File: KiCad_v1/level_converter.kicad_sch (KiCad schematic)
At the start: 3 parts, among them Q1 BSS138

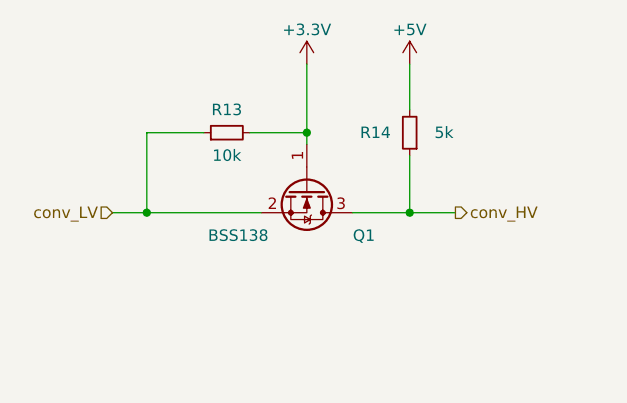
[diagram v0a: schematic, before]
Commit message: Level converter changed to 74LV1T34
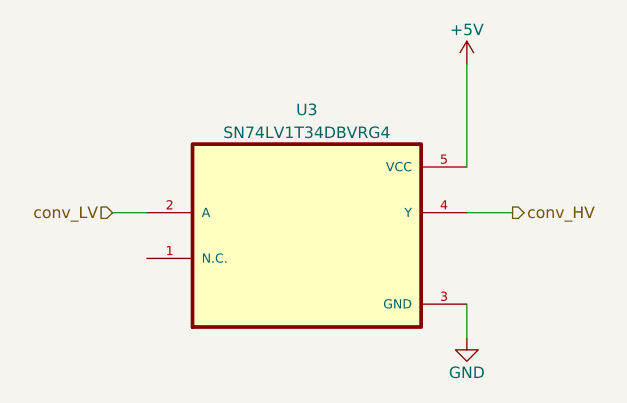
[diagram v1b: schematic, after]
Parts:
- removed Q1: BSS138, Package_TO_SOT_SMD:SOT-23, symbol Transistor_FET:BSS138
- removed R13: 10k, Resistor_SMD:R_0603_1608Metric_Pad0.98x0.95mm_HandSolder, symbol Device:R_Small
- removed R14: 5k, Resistor_SMD:R_0603_1608Metric_Pad0.98x0.95mm_HandSolder, symbol Device:R_Small
- added U3: SN74LV1T34DBVRG4, SOT95P280X145-5N, symbol sharp-ce140f-emul:SN74LV1T34DBVRG4
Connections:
- net +5V: now also U3.5 (VCC)
- net conv_HV: now also U3.4 (Y)
- net conv_LV: now also U3.2 (A)
- new net GND: U3.3 (GND)
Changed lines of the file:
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@@
-(kicad_sch (version 20211123) (generator eeschema)
+(kicad_sch (version 20230121) (generator eeschema)
   (paper "A5")
   (title_block
@@
     (rev "1")
     (comment 1 "https://www.sparkfun.com/products/12009")
-    (comment 2 "Bi-directional logic level converter")
+    (comment 2 "Single Power Supply Single Buffer GATE CMOS Logic Level Shifter")
   )
-  (junction (at 101.6 60.96) (diameter 0) (color 0 0 0 0)
+  (wire (pts (xy 119.38 69.85) (xy 124.46 69.85))
+    (stroke (width 0) (type default))
   )
-  (junction (at 83.82 69.85) (diameter 0) (color 0 0 0 0)
-  )
-  (junction (at 113.03 69.85) (diameter 0) (color 0 0 0 0)
-  )
-  (wire (pts (xy 113.03 69.85) (xy 118.11 69.85))
-    (stroke (width 0) (type default) (color 0 0 0 0))
-  )
-  (wire (pts (xy 83.82 60.96) (xy 90.17 60.96))
-    (stroke (width 0) (type default) (color 0 0 0 0))
-  )
-  (wire (pts (xy 113.03 53.34) (xy 113.03 58.42))
-    (stroke (width 0) (type default) (color 0 0 0 0))
-  )
-  (wire (pts (xy 95.25 60.96) (xy 101.6 60.96))
-    (stroke (width 0) (type default) (color 0 0 0 0))
-  )
-  (wire (pts (xy 101.6 53.34) (xy 101.6 60.96))
-    (stroke (width 0) (type default) (color 0 0 0 0))
-  )
-  (wire (pts (xy 113.03 63.5) (xy 113.03 69.85))
-    (stroke (width 0) (type default) (color 0 0 0 0))
-  )
-  (wire (pts (xy 83.82 69.85) (xy 96.52 69.85))
-    (stroke (width 0) (type default) (color 0 0 0 0))
-  )
-  (wire (pts (xy 101.6 60.96) (xy 101.6 62.23))
-    (stroke (width 0) (type default) (color 0 0 0 0))
-  )
-  (wire (pts (xy 83.82 69.85) (xy 83.82 60.96))
-    (stroke (width 0) (type default) (color 0 0 0 0))
-  )
-  (wire (pts (xy 106.68 69.85) (xy 113.03 69.85))
-    (stroke (width 0) (type default) (color 0 0 0 0))
+  (wire (pts (xy 119.38 80.01) (xy 119.38 83.82))
+    (stroke (width 0) (type default))
   )
   (wire (pts (xy 80.01 69.85) (xy 83.82 69.85))
-    (stroke (width 0) (type default) (color 0 0 0 0))
+    (stroke (width 0) (type default))
   )
-  (hierarchical_label "conv_HV" (shape output) (at 118.11 69.85 0)
+  (wire (pts (xy 119.38 53.34) (xy 119.38 64.77))
+    (stroke (width 0) (type default))
+  )
+  (hierarchical_label "conv_HV" (shape output) (at 124.46 69.85 0) (fields_autoplaced)
     (effects (font (size 1.27 1.27)) (justify left))
   )
-  (hierarchical_label "conv_LV" (shape input) (at 80.01 69.85 180)
+  (hierarchical_label "conv_LV" (shape input) (at 80.01 69.85 180) (fields_autoplaced)
     (effects (font (size 1.27 1.27)) (justify right))
   )
-  (symbol (lib_id "power:+5V") (at 113.03 53.34 0) (unit 1)
-    (in_bom yes) (on_board yes)
-    (property "Reference" "#PWR020" (id 0) (at 113.03 57.15 0)
+  (symbol (lib_id "power:+5V") (at 119.38 53.34 0) (unit 1)
+    (in_bom yes) (on_board yes) (dnp no)
+    (property "Reference" "#PWR020" (at 119.38 57.15 0)
       (effects (font (size 1.27 1.27)) hide)
     )
-    (property "Value" "+5V" (id 1) (at 113.03 49.53 0))
-    (property "Footprint" "" (id 2) (at 113.03 53.34 0)
+    (property "Value" "+5V" (at 119.38 49.53 0)
+      (effects (font (size 1.27 1.27)))
+    )
+    (property "Footprint" "" (at 119.38 53.34 0)
       (effects (font (size 1.27 1.27)) hide)
     )
-    (property "Datasheet" "" (id 3) (at 113.03 53.34 0)
+    (property "Datasheet" "" (at 119.38 53.34 0)
       (effects (font (size 1.27 1.27)) hide)
     )
     (pin "1")
+    (instances
+      (project "sharp-ce140f-emul_v1"
+        (path "/a1aa6218-39ed-4b37-9200-4448085ec785/ec3bcf54-6c70-4868-a3e2-d07f7ca44b3e"
+          (reference "#PWR020") (unit 1)
+        )
+        (path "/a1aa6218-39ed-4b37-9200-4448085ec785/a1077ba1-f425-4ad2-aac3-499598bb8fea"
+          (reference "#PWR0101") (unit 1)
+        )
+        (path "/a1aa6218-39ed-4b37-9200-4448085ec785/ce88f271-4809-4aaa-8ab4-efdfc9a3cf18"
+          (reference "#PWR0102") (unit 1)
+        )
+        (path "/a1aa6218-39ed-4b37-9200-4448085ec785/10a7e6a0-6c73-4880-bece-d370b7dbb5d0"
+          (reference "#PWR0103") (unit 1)
+        )
+        (path "/a1aa6218-39ed-4b37-9200-4448085ec785/f63beab0-aa70-4631-88ee-9ebb92c922a4"
+          (reference "#PWR0104") (unit 1)
+        )
+      )
+    )
   )
-  (symbol (lib_id "Device:R_Small") (at 92.71 60.96 90) (unit 1)
-    (in_bom yes) (on_board yes)
-    (property "Reference" "R13" (id 0) (at 92.71 58.42 90))
-    (property "Value" "10k" (id 1) (at 92.71 63.5 90))
-    (property "Footprint" "Resistor_SMD:R_0603_1608Metric_Pad0.98x0.95mm_HandSolder" (id 2) (at 92.71 60.96 0)
-      (effects (font (size 1.27 1.27)) hide)
+  (symbol (lib_id "sharp-ce140f-emul:SN74LV1T34DBVRG4") (at 101.6 72.39 0) (unit 1)
+    (in_bom yes) (on_board yes) (dnp no) (fields_autoplaced)
+    (property "Reference" "U3" (at 101.6 58.42 0)
+      (effects (font (size 1.27 1.27)))
     )
-    (property "Datasheet" "~" (id 3) (at 92.71 60.96 0)
+    (property "Value" "SN74LV1T34DBVRG4" (at 101.6 60.96 0)
+      (effects (font (size 1.27 1.27)))
+    )
+    (property "Footprint" "SOT95P280X145-5N" (at 101.6 72.39 0)
+      (effects (font (size 1.27 1.27)) (justify bottom) hide)
+    )
+    (property "Datasheet" "" (at 101.6 72.39 0)
       (effects (font (size 1.27 1.27)) hide)
     )
     (pin "1")
     (pin "2")
+    (pin "3")
+    (pin "4")
+    (pin "5")
+    (instances
+      (project "sharp-ce140f-emul_v1"
+        (path "/a1aa6218-39ed-4b37-9200-4448085ec785/ec3bcf54-6c70-4868-a3e2-d07f7ca44b3e"
+          (reference "U3") (unit 1)
+        )
+        (path "/a1aa6218-39ed-4b37-9200-4448085ec785/a1077ba1-f425-4ad2-aac3-499598bb8fea"
+          (reference "U4") (unit 1)
+        )
+        (path "/a1aa6218-39ed-4b37-9200-4448085ec785/ce88f271-4809-4aaa-8ab4-efdfc9a3cf18"
+          (reference "U5") (unit 1)
+        )
+        (path "/a1aa6218-39ed-4b37-9200-4448085ec785/10a7e6a0-6c73-4880-bece-d370b7dbb5d0"
+          (reference "U6") (unit 1)
+        )
+        (path "/a1aa6218-39ed-4b37-9200-4448085ec785/f63beab0-aa70-4631-88ee-9ebb92c922a4"
+          (reference "U7") (unit 1)
+        )
+      )
+    )
   )
-  (symbol (lib_id "Transistor_FET:BSS138") (at 101.6 67.31 270) (unit 1)
-    (in_bom yes) (on_board yes)
-    (property "Reference" "Q1" (id 0) (at 107.95 72.39 90))
-    (property "Value" "BSS138" (id 1) (at 93.98 72.39 90))
-    (property "Footprint" "Package_TO_SOT_SMD:SOT-23" (id 2) (at 99.695 72.39 0)
-      (effects (font (size 1.27 1.27) italic) (justify left) hide)
-    )
-    (property "Datasheet" "https://www.onsemi.com/pub/Collateral/BSS138-D.PDF" (id 3) (at 101.6 67.31 0)
-      (effects (font (size 1.27 1.27)) (justify left) hide)
-    )
-    (pin "1")
-    (pin "2")
-    (pin "3")
-  )
-  (symbol (lib_id "power:+3.3V") (at 101.6 53.34 0) (unit 1)
-    (in_bom yes) (on_board yes)
-    (property "Reference" "#PWR019" (id 0) (at 101.6 57.15 0)
+  (symbol (lib_id "power:GND") (at 119.38 83.82 0) (mirror y) (unit 1)
+    (in_bom yes) (on_board yes) (dnp no)
+    (property "Reference" "#PWR07" (at 119.38 90.17 0)
       (effects (font (size 1.27 1.27)) hide)
     )
-    (property "Value" "+3.3V" (id 1) (at 101.6 49.53 0))
-    (property "Footprint" "" (id 2) (at 101.6 53.34 0)
+    (property "Value" "GND" (at 119.38 87.63 0)
+      (effects (font (size 1.27 1.27)))
+    )
+    (property "Footprint" "" (at 119.38 83.82 0)
       (effects (font (size 1.27 1.27)) hide)
     )
-    (property "Datasheet" "" (id 3) (at 101.6 53.34 0)
+    (property "Datasheet" "" (at 119.38 83.82 0)
       (effects (font (size 1.27 1.27)) hide)
     )
     (pin "1")
-  )
-  (symbol (lib_id "Device:R_Small") (at 113.03 60.96 180) (unit 1)
-    (in_bom yes) (on_board yes)
-    (property "Reference" "R14" (id 0) (at 109.22 60.96 0))
-    (property "Value" "5k" (id 1) (at 116.84 60.96 0))
-    (property "Footprint" "Resistor_SMD:R_0603_1608Metric_Pad0.98x0.95mm_HandSolder" (id 2) (at 113.03 60.96 0)
-      (effects (font (size 1.27 1.27)) hide)
+    (instances
+      (project "sharp-ce140f-emul_v1"
+        (path "/a1aa6218-39ed-4b37-9200-4448085ec785"
+          (reference "#PWR07") (unit 1)
+        )
+        (path "/a1aa6218-39ed-4b37-9200-4448085ec785/ec3bcf54-6c70-4868-a3e2-d07f7ca44b3e"
+          (reference "#PWR019") (unit 1)
+        )
+        (path "/a1aa6218-39ed-4b37-9200-4448085ec785/a1077ba1-f425-4ad2-aac3-499598bb8fea"
+          (reference "#PWR021") (unit 1)
+        )
+        (path "/a1aa6218-39ed-4b37-9200-4448085ec785/ce88f271-4809-4aaa-8ab4-efdfc9a3cf18"
+          (reference "#PWR022") (unit 1)
+        )
+        (path "/a1aa6218-39ed-4b37-9200-4448085ec785/10a7e6a0-6c73-4880-bece-d370b7dbb5d0"
+          (reference "#PWR023") (unit 1)
+        )
+        (path "/a1aa6218-39ed-4b37-9200-4448085ec785/f63beab0-aa70-4631-88ee-9ebb92c922a4"
+          (reference "#PWR024") (unit 1)
+        )
+      )
     )
-    (property "Datasheet" "~" (id 3) (at 113.03 60.96 0)
-      (effects (font (size 1.27 1.27)) hide)
-    )
-    (pin "1")
-    (pin "2")
   )
 )
